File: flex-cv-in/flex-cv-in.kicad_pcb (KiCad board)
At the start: 2 copper layers, 30 x 17 mm, 19 parts, among them J1 3.5mm_Mono_Switched, J2 HDR, U1 TLV9061xDBV

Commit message: Update to final Rev. A
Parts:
- added TP1: TP_VREF, TestPoint:TestPoint_Pad_D1.5mm, F.Cu at (133.0, 63.3)
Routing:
- net /VREF_1.65V: track 27.7 -> 29.9 mm
- net GND: vias 14 -> 15
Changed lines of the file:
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@@
 		(property ki_fp_filters "R_*")
 		(sheetname "/")
-		(sheetfile "biased-CV-input-unity.kicad_sch")
+		(sheetfile "flex-cv-in.kicad_sch")
 		(attr smd)
 		(fp_line
@@
 		(property ki_fp_filters "C_*")
 		(sheetname "/")
-		(sheetfile "biased-CV-input-unity.kicad_sch")
+		(sheetfile "flex-cv-in.kicad_sch")
 		(attr smd)
 		(fp_line
@@
 		(property ki_fp_filters "SolderJumper*Bridged*")
 		(sheetname "/")
-		(sheetfile "biased-CV-input-unity.kicad_sch")
+		(sheetfile "flex-cv-in.kicad_sch")
 		(zone_connect 1)
 		(attr exclude_from_pos_files exclude_from_bom allow_soldermask_bridges)
@@
 		(property ki_fp_filters "Connector*:*_1x??_*")
 		(sheetname "/")
-		(sheetfile "biased-CV-input-unity.kicad_sch")
-		(attr through_hole exclude_from_pos_files)
+		(sheetfile "flex-cv-in.kicad_sch")
+		(attr through_hole exclude_from_pos_files exclude_from_bom)
 		(fp_line
 			(start -1.38 9)
@@
 		(property ki_fp_filters "C_*")
 		(sheetname "/")
-		(sheetfile "biased-CV-input-unity.kicad_sch")
+		(sheetfile "flex-cv-in.kicad_sch")
 		(attr smd)
 		(fp_line
@@
 		(property ki_fp_filters "R_*")
 		(sheetname "/")
-		(sheetfile "biased-CV-input-unity.kicad_sch")
+		(sheetfile "flex-cv-in.kicad_sch")
 		(attr smd)
 		(fp_line
@@
 		(property ki_fp_filters "SolderJumper*Open*")
 		(sheetname "/")
-		(sheetfile "biased-CV-input-unity.kicad_sch")
+		(sheetfile "flex-cv-in.kicad_sch")
 		(zone_connect 1)
 		(attr exclude_from_pos_files exclude_from_bom allow_soldermask_bridges)
@@
 		(property ki_fp_filters "R_*")
 		(sheetname "/")
-		(sheetfile "biased-CV-input-unity.kicad_sch")
+		(sheetfile "flex-cv-in.kicad_sch")
 		(attr smd)
 		(fp_line
@@
 		)
 	)
+	(footprint "TestPoint:TestPoint_Pad_D1.5mm"
+		(layer "F.Cu")
+		(at 133 63.3)
+		(descr "SMD pad as test Point, diameter 1.5mm")
+		(tags "test point SMD pad")
+		(property "Reference" "TP1"
+			(at 0 1.8 0)
+			(layer "F.SilkS")
+			(effects
+				(font
+					(size 1 1)
+					(thickness 0.15)
+				)
+			)
+		)
+		(property "Value" "TP_VREF"
+			(at 0 -2.8 0)
+			(layer "F.Fab")
+			(effects
+				(font
+					(size 1 1)
+					(thickness 0.15)
+				)
+			)
+		)
+		(property "Datasheet" ""
+			(at 0 0 0)
+			(unlocked yes)
+			(layer "F.Fab")
+			(hide yes)
+			(effects
+				(font
+					(size 1.27 1.27)
+					(thickness 0.15)
+				)
+			)
+		)
+		(property "Description" ""
+			(at 0 0 0)
+			(unlocked yes)
+			(layer "F.Fab")
+			(hide yes)
+			(effects
+				(font
+					(size 1.27 1.27)
+					(thickness 0.15)
+				)
+			)
+		)
+		(property ki_fp_filters "Pin* Test*")
+		(sheetname "/")
+		(sheetfile "flex-cv-in.kicad_sch")
+		(attr exclude_from_pos_files exclude_from_bom)
+		(fp_circle
+			(center 0 0)
+			(end 0 0.95)
+			(stroke
+				(width 0.12)
+				(type solid)
+			)
+			(fill no)
+			(layer "F.SilkS")
+		)
+		(fp_circle
+			(center 0 0)
+			(end 1.25 0)
+			(stroke
+				(width 0.05)
+				(type solid)
+			)
+			(fill no)
+			(layer "F.CrtYd")
+		)
+		(fp_text user "${REFERENCE}"
+			(at 0.7 2.5 0)
+			(layer "F.Fab")
+			(effects
+				(font
+					(size 1 1)
+					(thickness 0.15)
+				)
+			)
+		)
+		(pad "1" smd circle
+			(at 0 0)
+			(size 1.5 1.5)
+			(layers "F.Cu" "F.Mask")
+			(net 3 "/VREF_1.65V")
+			(pinfunction "1")
+			(pintype "passive")
+		)
+		(embedded_fonts no)
+	)
 	(footprint "Package_TO_SOT_SMD:SOT-23-5"
 		(layer "F.Cu")
@@
 		(property ki_fp_filters "SOT?23*")
 		(sheetname "/")
-		(sheetfile "biased-CV-input-unity.kicad_sch")
+		(sheetfile "flex-cv-in.kicad_sch")
 		(attr smd)
 		(fp_line
@@
 		(property ki_fp_filters "R_*")
 		(sheetname "/")
-		(sheetfile "biased-CV-input-unity.kicad_sch")
+		(sheetfile "flex-cv-in.kicad_sch")
 		(attr smd)
 		(fp_line
@@
 		(property ki_fp_filters "C_*")
 		(sheetname "/")
-		(sheetfile "biased-CV-input-unity.kicad_sch")
+		(sheetfile "flex-cv-in.kicad_sch")
 		(attr smd)
 		(fp_line
@@
 		(property ki_fp_filters "SOT?23*")
 		(sheetname "/")
-		(sheetfile "biased-CV-input-unity.kicad_sch")
+		(sheetfile "flex-cv-in.kicad_sch")
 		(attr smd)
 		(fp_line
@@
 		(property ki_fp_filters "R_*")
 		(sheetname "/")
-		(sheetfile "biased-CV-input-unity.kicad_sch")
+		(sheetfile "flex-cv-in.kicad_sch")
 		(attr smd)
 		(fp_line
@@
 		(property ki_fp_filters "SolderJumper*Open*")
 		(sheetname "/")
-		(sheetfile "biased-CV-input-unity.kicad_sch")
+		(sheetfile "flex-cv-in.kicad_sch")
 		(zone_connect 1)
 		(attr exclude_from_pos_files exclude_from_bom allow_soldermask_bridges)
@@
 		(property ki_fp_filters "R_*")
 		(sheetname "/")
-		(sheetfile "biased-CV-input-unity.kicad_sch")
+		(sheetfile "flex-cv-in.kicad_sch")
 		(attr smd)
 		(fp_line
@@
 		(property ki_fp_filters "C_*")
 		(sheetname "/")
-		(sheetfile "biased-CV-input-unity.kicad_sch")
+		(sheetfile "flex-cv-in.kicad_sch")
 		(attr smd)
 		(fp_line
@@
 		(property ki_fp_filters "R_*")
 		(sheetname "/")
-		(sheetfile "biased-CV-input-unity.kicad_sch")
+		(sheetfile "flex-cv-in.kicad_sch")
 		(attr smd)
 		(fp_line
@@
 		)
 		(sheetname "/")
-		(sheetfile "biased-CV-input-unity.kicad_sch")
-		(attr through_hole exclude_from_pos_files)
+		(sheetfile "flex-cv-in.kicad_sch")
+		(attr through_hole exclude_from_pos_files exclude_from_bom)
 		(fp_line
 			(start -6.223 -5.0292)
@@
 		(property ki_fp_filters "Potentiometer*")
 		(sheetname "/")
-		(sheetfile "biased-CV-input-unity.kicad_sch")
-		(attr through_hole exclude_from_pos_files)
+		(sheetfile "flex-cv-in.kicad_sch")
+		(attr through_hole exclude_from_pos_files exclude_from_bom)
 		(fp_line
 			(start -4.41 -5.5)
@@
 	)
 	(gr_line
+		(start 121.2 67.25)
+		(end 120.9 67.75)
+		(stroke
+			(width 0.15)
+			(type solid)
+		)
+		(layer "F.SilkS")
+	)
+	(gr_line
+		(start 120.9 67.75)
+		(end 121.5 67.75)
+		(stroke
+			(width 0.15)
+			(type solid)
+		)
+		(layer "F.SilkS")
+	)
+	(gr_line
+		(start 121.5 67.75)
+		(end 121.2 67.25)
+		(stroke
+			(width 0.15)
+			(type solid)
+		)
+		(layer "F.SilkS")
+	)
+	(gr_line
 		(start 105 71)
 		(end 105 66)
@@
 	)
 	(via
-		(at 106.6 65.8)
+		(at 133.1 65.7)
 		(size 0.6)
 		(drill 0.3)
@@
 	)
 	(via
-		(at 132.2 74.6)
+		(at 106.6 65.8)
 		(size 0.6)
 		(drill 0.3)
@@
 	)
 	(via
-		(at 127.8 72.4)
+		(at 132.2 74.6)
 		(size 0.6)
 		(drill 0.3)
@@
 	)
 	(via
-		(at 133 64.2)
+		(at 127.8 72.4)
 		(size 0.6)
 		(drill 0.3)
@@
 	)
 	(via
+		(at 132.2 61.9)
+		(size 0.6)
+		(drill 0.3)
+		(layers "F.Cu" "B.Cu")
+		(free yes)
+		(net 2)
+	)
+	(via
 		(at 106.4 71)
 		(size 0.6)
@@
 	)
 	(segment
+		(start 131.4 64.6)
+		(end 131.4 63.8125)
+		(width 0.3)
+		(layer "F.Cu")
+		(net 3)
+	)
+	(segment
+		(start 131.6 64.6)
+		(end 133 63.2)
+		(width 0.3)
+		(layer "F.Cu")
+		(net 3)
+	)
+	(segment
+		(start 131.4 64.6)
+		(end 131.6 64.6)
+		(width 0.3)
+		(layer "F.Cu")
+		(net 3)
+	)
+	(segment
 		(start 124.75 63.1625)
 		(end 130.75 63.1625)
@@
 	(segment
 		(start 131.4 66.760163)
-		(end 131.4 63.8125)
+		(end 131.4 64.6)
 		(width 0.3)
 		(layer "F.Cu")

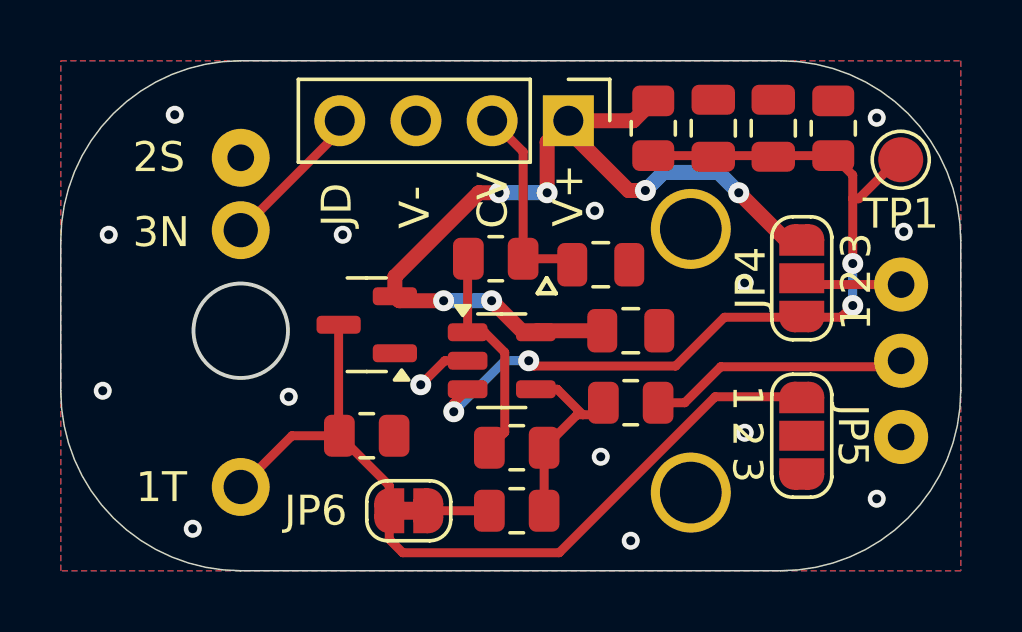
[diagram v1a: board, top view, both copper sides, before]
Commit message: flex-cv-in rev. B
Updates and bug fixes:

- Removed jack detect
- Changed R7 connection from GND to VREF_1.65V
- Connected JP5 pad 2 to RV2 pad 3
- Adjusted layout of JP6 to avoid inadvertently cutting CV_IN trace
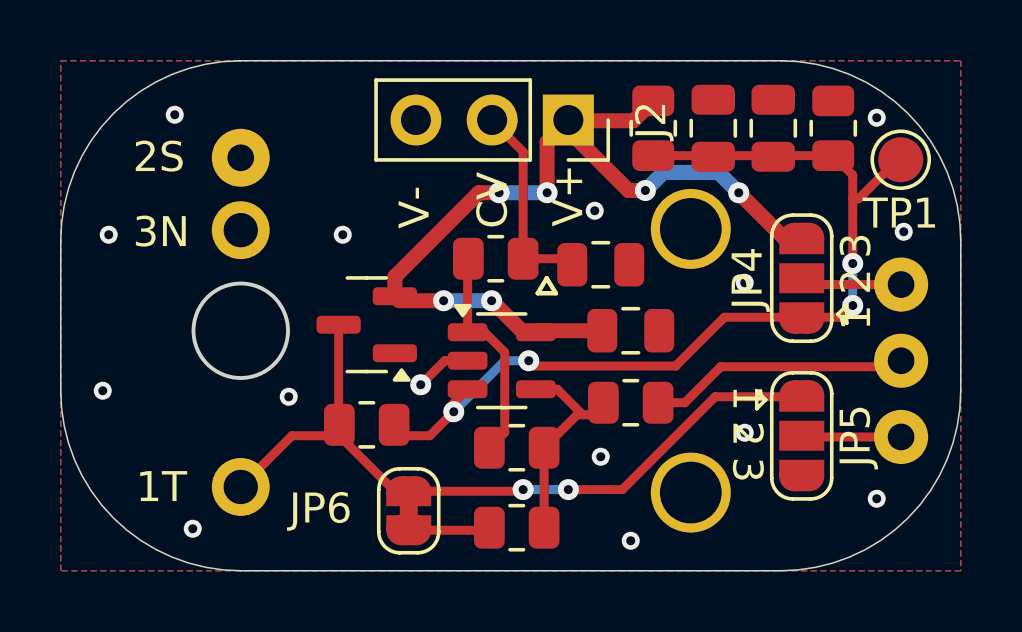
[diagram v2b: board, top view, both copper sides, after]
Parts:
- J2: footprint Connector_PinHeader_2.54mm:PinHeader_1x04_P2.54mm_Vertical -> Connector_PinSocket_2.54mm:PinSocket_1x03_P2.54mm_Vertical
- JP4, JP5: footprint Jumper:SolderJumper-3_P1.3mm_Open_RoundedPad1.0x1.5mm -> elemental_jumper:SolderJumper-3_P1.3mm_Open_RoundedPad1.0x1.5mm
- moved R2 0.56 mm to (120.2, 75.6)
- moved R7 0.36 mm to (115.2, 72.1)
- turned JP6 to 90 degrees
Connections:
- J1 pad 3: /JACK_DETECT -> unconnected-(J1-SW-Pad3)
- R7 pad 1: GND -> /VREF_1.65V
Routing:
- net /JACK_DETECT: track 5.01 -> 0.00 mm
- net Net-(JP5-C): track 0.00 -> 3.33 mm
- net /CV_IN: track 27.9 -> 25.3 mm, vias 0 -> 2
- net /VREF_1.65V: track 29.9 -> 32.3 mm
- net /R_IN: track 2.04 -> 2.72 mm
- net /SUMMED_CV_IN: track 6.73 -> 7.29 mm
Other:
- board text added: "rev B"
- board text removed: "JD"
- board text removed: "rev A"

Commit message: update JLC production files
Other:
- board text added: "flex-cv-in"
- board text removed: "cv-in-flex"
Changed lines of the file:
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@@
 		(sheetname "/")
 		(sheetfile "flex-cv-in.kicad_sch")
-		(attr through_hole)
+		(attr through_hole exclude_from_pos_files exclude_from_bom)
 		(fp_line
 			(start -1.33 6.41)
@@
 		(sheetname "/")
 		(sheetfile "flex-cv-in.kicad_sch")
-		(attr exclude_from_pos_files)
+		(attr exclude_from_pos_files exclude_from_bom)
 		(fp_circle
 			(center 0 0)
@@
 		(sheetname "/")
 		(sheetfile "flex-cv-in.kicad_sch")
-		(attr through_hole exclude_from_pos_files)
+		(attr through_hole exclude_from_pos_files exclude_from_bom)
 		(fp_line
 			(start -6.223 -5.0292)
@@
 		(sheetname "/")
 		(sheetfile "flex-cv-in.kicad_sch")
-		(attr through_hole exclude_from_pos_files)
+		(attr through_hole exclude_from_pos_files exclude_from_bom)
 		(fp_line
 			(start -4.41 -5.5)
@@
 		)
 	)
-	(gr_text "cv-in-flex"
+	(gr_text "flex-cv-in"
 		(at 131.8 63.2 0)
 		(layer "B.SilkS")
@@
 			(justify left bottom mirror)
 		)
-		(render_cache "cv-in-flex" 0
+		(render_cache "flex-cv-in" 0
 			(polygon
 				(pts
-					(xy 131.108304 63.03) (xy 131.596118 63.03) (xy 131.737473 62.888705) (xy 131.737473 62.471782)
-					(xy 131.596118 62.330488) (xy 131.108304 62.330488) (xy 131.108304 62.439603) (xy 131.547208 62.439603)
-					(xy 131.625488 62.517944) (xy 131.625488 62.842543) (xy 131.547208 62.920884) (xy 131.108304 62.920884)
+					(xy 130.803489 63.03) (xy 131.252896 63.03) (xy 131.252896 62.920884) (xy 131.083513 62.920884)
+					(xy 131.083513 62.158236) (xy 131.461967 62.158236) (xy 131.539515 62.237187) (xy 131.539515 62.486803)
+					(xy 131.237264 62.486803) (xy 131.237264 62.595919) (xy 131.539515 62.595919) (xy 131.539515 63.03)
+					(xy 131.6515 63.03) (xy 131.6515 62.595919) (xy 131.792184 62.595919) (xy 131.792184 62.486803)
+					(xy 131.6515 62.486803) (xy 131.6515 62.190659) (xy 131.51045 62.04912) (xy 130.971528 62.04912)
+					(xy 130.971528 62.920884) (xy 130.803489 62.920884)
 				)
 			)
 			(polygon
 				(pts
-					(xy 130.311095 62.330488) (xy 130.311095 62.747411) (xy 130.593745 63.03) (xy 130.727957 63.03)
-					(xy 131.010607 62.747411) (xy 131.010607 62.330488) (xy 130.898621 62.330488) (xy 130.898621 62.701249)
-					(xy 130.679047 62.920884) (xy 130.642655 62.920884) (xy 130.42308 62.701249) (xy 130.42308 62.330488)
+					(xy 130.713607 62.471477) (xy 130.713607 62.8884) (xy 130.572252 63.03) (xy 130.056106 63.03) (xy 130.056106 62.920884)
+					(xy 130.523281 62.920884) (xy 130.601622 62.841749) (xy 130.601622 62.733) (xy 130.014096 62.733)
+					(xy 130.014096 62.517212) (xy 130.126081 62.517212) (xy 130.126081 62.623885) (xy 130.601622 62.623885)
+					(xy 130.601622 62.517212) (xy 130.523281 62.439603) (xy 130.204422 62.439603) (xy 130.126081 62.517212)
+					(xy 130.014096 62.517212) (xy 130.014096 62.471477) (xy 130.155451 62.330488) (xy 130.572252 62.330488)
 				)
 			)
 			(polygon
 				(pts
-					(xy 129.745429 62.666566) (xy 130.163572 62.666566) (xy 130.163572 62.557451) (xy 129.745429 62.557451)
+					(xy 129.221772 62.897254) (xy 129.221772 63.03) (xy 129.333757 63.03) (xy 129.333757 62.943843)
+					(xy 129.530983 62.744724) (xy 129.612072 62.744724) (xy 129.809298 62.943843) (xy 129.809298 63.03)
+					(xy 129.921284 63.03) (xy 129.921284 62.897254) (xy 129.702991 62.67829) (xy 129.921284 62.461402)
+					(xy 129.921284 62.330488) (xy 129.809298 62.330488) (xy 129.809298 62.415484) (xy 129.612072 62.611856)
+					(xy 129.530983 62.611856) (xy 129.333757 62.412676) (xy 129.333757 62.330488) (xy 129.221772 62.330488)
+					(xy 129.221772 62.461402) (xy 129.440064 62.67829)
 				)
 			)
 			(polygon
 				(pts
-					(xy 129.229588 63.03) (xy 129.678995 63.03) (xy 129.678995 62.920884) (xy 129.510956 62.920884)
-					(xy 129.510956 62.439603) (xy 129.678995 62.439603) (xy 129.678995 62.330488) (xy 129.39897 62.330488)
-					(xy 129.39897 62.920884) (xy 129.229588 62.920884)
+					(xy 128.672714 62.666566) (xy 129.090858 62.666566) (xy 129.090858 62.557451) (xy 128.672714 62.557451)
 				)
 			)
 			(polygon
 				(pts
-					(xy 129.39897 62.162449) (xy 129.510956 62.162449) (xy 129.510956 62.04912) (xy 129.39897 62.04912)
+					(xy 127.887229 63.03) (xy 128.375043 63.03) (xy 128.516399 62.888705) (xy 128.516399 62.471782)
+					(xy 128.375043 62.330488) (xy 127.887229 62.330488) (xy 127.887229 62.439603) (xy 128.326133 62.439603)
+					(xy 128.404413 62.517944) (xy 128.404413 62.842543) (xy 128.326133 62.920884) (xy 127.887229 62.920884)
 				)
 			)
 			(polygon
 				(pts
-					(xy 128.421632 63.03) (xy 128.533618 63.03) (xy 128.533618 62.517944) (xy 128.611959 62.439603)
-					(xy 129.009159 62.439603) (xy 129.009159 63.03) (xy 129.121144 63.03) (xy 129.121144 62.330488)
-					(xy 128.562988 62.330488) (xy 128.421632 62.471782)
+					(xy 127.09002 62.330488) (xy 127.09002 62.747411) (xy 127.37267 63.03) (xy 127.506882 63.03) (xy 127.789532 62.747411)
+					(xy 127.789532 62.330488) (xy 127.677547 62.330488) (xy 127.677547 62.701249) (xy 127.457972 62.920884)
+					(xy 127.42158 62.920884) (xy 127.202006 62.701249) (xy 127.202006 62.330488)
 				)
 			)
 			(polygon
 				(pts
-					(xy 127.841311 62.666566) (xy 128.259455 62.666566) (xy 128.259455 62.557451) (xy 127.841311 62.557451)
+					(xy 126.524354 62.666566) (xy 126.942498 62.666566) (xy 126.942498 62.557451) (xy 126.524354 62.557451)
 				)
 			)
 			(polygon
 				(pts
-					(xy 126.751011 63.03) (xy 127.200418 63.03) (xy 127.200418 62.920884) (xy 127.031036 62.920884)
-					(xy 127.031036 62.158236) (xy 127.40949 62.158236) (xy 127.487037 62.237187) (xy 127.487037 62.486803)
-					(xy 127.184787 62.486803) (xy 127.184787 62.595919) (xy 127.487037 62.595919) (xy 127.487037 63.03)
-					(xy 127.599023 63.03) (xy 127.599023 62.595919) (xy 127.739706 62.595919) (xy 127.739706 62.486803)
-					(xy 127.599023 62.486803) (xy 127.599023 62.190659) (xy 127.457972 62.04912) (xy 126.91905 62.04912)
-					(xy 126.91905 62.920884) (xy 126.751011 62.920884)
+					(xy 126.008513 63.03) (xy 126.45792 63.03) (xy 126.45792 62.920884) (xy 126.289881 62.920884) (xy 126.289881 62.439603)
+					(xy 126.45792 62.439603) (xy 126.45792 62.330488) (xy 126.177896 62.330488) (xy 126.177896 62.920884)
+					(xy 126.008513 62.920884)
 				)
 			)
 			(polygon
 				(pts
-					(xy 126.66113 62.471477) (xy 126.66113 62.8884) (xy 126.519774 63.03) (xy 126.003628 63.03) (xy 126.003628 62.920884)
-					(xy 126.470804 62.920884) (xy 126.549145 62.841749) (xy 126.549145 62.733) (xy 125.961618 62.733)
-					(xy 125.961618 62.517212) (xy 126.073604 62.517212) (xy 126.073604 62.623885) (xy 126.549145 62.623885)
-					(xy 126.549145 62.517212) (xy 126.470804 62.439603) (xy 126.151945 62.439603) (xy 126.073604 62.517212)
-					(xy 125.961618 62.517212) (xy 125.961618 62.471477) (xy 126.102974 62.330488) (xy 126.519774 62.330488)
+					(xy 126.177896 62.162449) (xy 126.289881 62.162449) (xy 126.289881 62.04912) (xy 126.177896 62.04912)
 				)
 			)
 			(polygon
 				(pts
-					(xy 125.169295 62.897254) (xy 125.169295 63.03) (xy 125.28128 63.03) (xy 125.28128 62.943843) (xy 125.478506 62.744724)
-					(xy 125.559595 62.744724) (xy 125.756821 62.943843) (xy 125.756821 63.03) (xy 125.868806 63.03)
-					(xy 125.868806 62.897254) (xy 125.650514 62.67829) (xy 125.868806 62.461402) (xy 125.868806 62.330488)
-					(xy 125.756821 62.330488) (xy 125.756821 62.415484) (xy 125.559595 62.611856) (xy 125.478506 62.611856)
-					(xy 125.28128 62.412676) (xy 125.28128 62.330488) (xy 125.169295 62.330488) (xy 125.169295 62.461402)
-					(xy 125.387587 62.67829)
+					(xy 125.200558 63.03) (xy 125.312543 63.03) (xy 125.312543 62.517944) (xy 125.390884 62.439603)
+					(xy 125.788084 62.439603) (xy 125.788084 63.03) (xy 125.900069 63.03) (xy 125.900069 62.330488)
+					(xy 125.341913 62.330488) (xy 125.200558 62.471782)
 				)
 			)
